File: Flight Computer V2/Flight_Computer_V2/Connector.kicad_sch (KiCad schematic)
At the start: 6 parts, among them J101 Conn_02x26_Odd_Even, J102 Conn_02x26_Odd_Even

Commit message: finalized schematic, added datasheets, and pdf of schematic
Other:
- company: (none) -> By: Dylan Haussecker
- title: (none) -> Avionics Flight Computer
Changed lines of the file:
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@@
 (kicad_sch (version 20230121) (generator eeschema)
   (paper "A4")
+  (title_block
+    (title "Avionics Flight Computer")
+    (date "2023-09-04")
+    (rev "1.0")
+    (company "By: Dylan Haussecker")
+  )
   (junction (at 102.87 109.22) (diameter 0) (color 0 0 0 0)
   )

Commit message: updated pcb
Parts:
- removed JP1 (x2): ~, symbol Jumper:SolderJumper_2_Open
- R501, R502: footprint Capacitor_SMD:C_0603_1608Metric_Pad1.08x0.95mm_HandSolder -> Resistor_SMD:R_0603_1608Metric
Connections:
- net +3.3V: no longer J102.27 (Pin_27), J102.28 (Pin_28)
- net SCL: now also J101.43 (Pin_43), R502.2
- net SDA: now also J101.41 (Pin_41), R501.2
- net +5V renamed 5VIN
- new net 3V3IN: J102.27 (Pin_27), J102.28 (Pin_28)

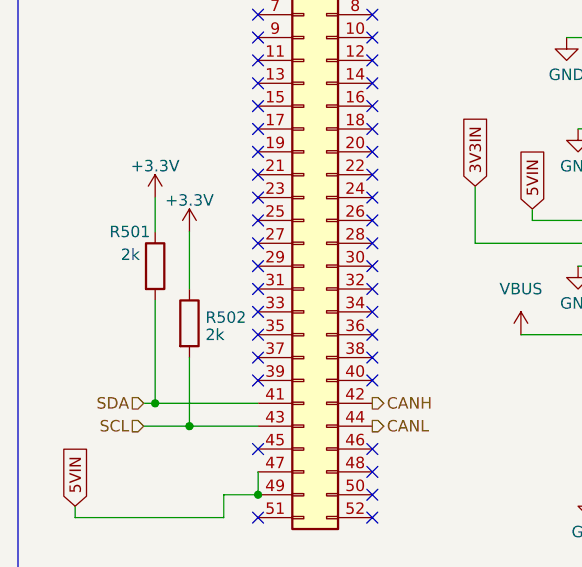
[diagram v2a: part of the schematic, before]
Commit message: changed new flight computer scl resistors
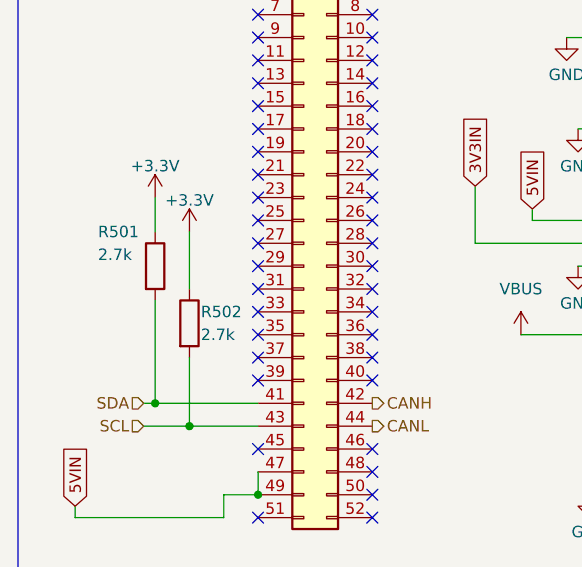
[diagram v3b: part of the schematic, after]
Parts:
- R501, R502: value 2k -> 2.7k
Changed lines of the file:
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@@
   (symbol (lib_id "Device:R") (at 99.06 93.98 0) (unit 1)
     (in_bom yes) (on_board yes) (dnp no)
-    (property "Reference" "R501" (at 93.98 90.17 0)
-      (effects (font (size 1.27 1.27)) (justify left))
-    )
-    (property "Value" "2k" (at 95.25 92.71 0)
+    (property "Reference" "R501" (at 92.71 90.17 0)
+      (effects (font (size 1.27 1.27)) (justify left))
+    )
+    (property "Value" "2.7k" (at 92.71 92.71 0)
       (effects (font (size 1.27 1.27)) (justify left))
     )
@@
   )
   (symbol (lib_id "Device:R") (at 102.87 100.33 0) (unit 1)
-    (in_bom yes) (on_board yes) (dnp no) (fields_autoplaced)
-    (property "Reference" "R502" (at 104.648 99.6863 0)
-      (effects (font (size 1.27 1.27)) (justify left))
-    )
-    (property "Value" "2k" (at 104.648 101.6073 0)
-      (effects (font (size 1.27 1.27)) (justify left))
-    )
+    (in_bom yes) (on_board yes) (dnp no)
+    (property "Reference" "R502" (at 104.14 99.06 0)
+      (effects (font (size 1.27 1.27)) (justify left))
+    )
+    (property "Value" "2.7k" (at 104.14 101.6 0)
+      (effects (font (size 1.27 1.27)) (justify left))
+    )
